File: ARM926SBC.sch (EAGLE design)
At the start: 53 parts, among them IC1 AT91SAM9260B-QU, IC2 LP2985IM5X-1.8, IC3 LM3671MF-1.8, IC4 LM3671MF-3.3, IC5 LP2985IM5X-3.3, Q1 2N7002, X1 16M, X2 32768

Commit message: Semi-finished: SDRAM and NAND
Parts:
- added IC6: MT48LC32M16A2-75C, ARM926SBC:MT48LC32M16A2-75C
- added IC7: K9F4G08U0B-P, ARM926SBC:K9F4G08U0B-P
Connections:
- new net A0: IC1-EBI.A2, IC6.A0
- new net A1: IC1-EBI.A3, IC6.A1
- new net A10: IC1-EBI.SDA10, IC6.A10
- new net A11: IC1-EBI.A13, IC6.A11
- new net A12: IC1-EBI.A14, IC6.A12
- new net A2: IC1-EBI.A4, IC6.A2
- new net A3: IC1-EBI.A5, IC6.A3
- new net A4: IC1-EBI.A6, IC6.A4
- new net A5: IC1-EBI.A7, IC6.A5
- new net A6: IC1-EBI.A8, IC6.A6
- new net A7: IC1-EBI.A9, IC6.A7
- new net A8: IC1-EBI.A10, IC6.A8
- new net A9: IC1-EBI.A11, IC6.A9
- new net BA0: IC1-EBI.A16/BA0, IC6.BA0
- new net BA1: IC1-EBI.A17/BA1, IC6.BA1
- new net CS0: IC1-EBI.CS#0
- new net CS1: IC1-EBI.CS#1, IC6.CS#
- new net CS3: IC1-PORTC.PC14/CS#3/IRQ2, IC7.CE#
- new net D0: IC1-EBI.D0, IC6.D0, IC7.D0
- new net D1: IC1-EBI.D1, IC6.D1, IC7.D1
- new net D10: IC1-EBI.D10, IC6.D10
- new net D11: IC1-EBI.D11, IC6.D11
- new net D12: IC1-EBI.D12, IC6.D12
- new net D13: IC1-EBI.D13, IC6.D13
- new net D14: IC1-EBI.D14, IC6.D14
- new net D15: IC1-EBI.D15, IC6.D15
- new net D2: IC1-EBI.D2, IC6.D2, IC7.D2
- new net D3: IC1-EBI.D3, IC6.D3, IC7.D3
- new net D4: IC1-EBI.D4, IC6.D4, IC7.D4
- new net D5: IC1-EBI.D5, IC6.D5, IC7.D5
- new net D6: IC1-EBI.D6, IC6.D6, IC7.D6
- new net D7: IC1-EBI.D7, IC6.D7, IC7.D7
- new net D8: IC1-EBI.D8, IC6.D8
- new net D9: IC1-EBI.D9, IC6.D9
- new net DQM0: IC1-EBI.BS#0/A0, IC6.DQML
- new net DQM1: IC1-EBI.BS#1/WR#1, IC6.DQMH
- new net DQM2: IC1-EBI.WR#2/BS#2/A1
- new net DQM3: IC1-EBI.BS#3/WR#3
- new net NALE: IC7.ALE
- new net NCLE: IC7.CLE
- new net NRD: IC1-EBI.NAND_RD, IC7.RD#
- new net NWR: IC1-EBI.NAND_WR, IC7.WR#
- new net SDCAS: IC1-EBI.CAS, IC6.CAS#
- new net SDCKE: IC1-EBI.SDCKE, IC6.CKE
- new net SDCLK: IC1-EBI.SDCK, IC6.CLK
- new net SDRAS: IC1-EBI.RAS, IC6.RAS#
- new net SDWE: IC1-EBI.SDWE, IC6.WE#
- new net SRD: IC1-EBI.RD#
- new net SWR: IC1-EBI.WR#
- net GND: now also IC6.GND, IC6.GNDQ, IC7.GND
- net VDD: now also IC6.VDD, IC6.VDDQ, IC7.VDD, IC7.WP#
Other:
- note added: "SDRAM and NAND"

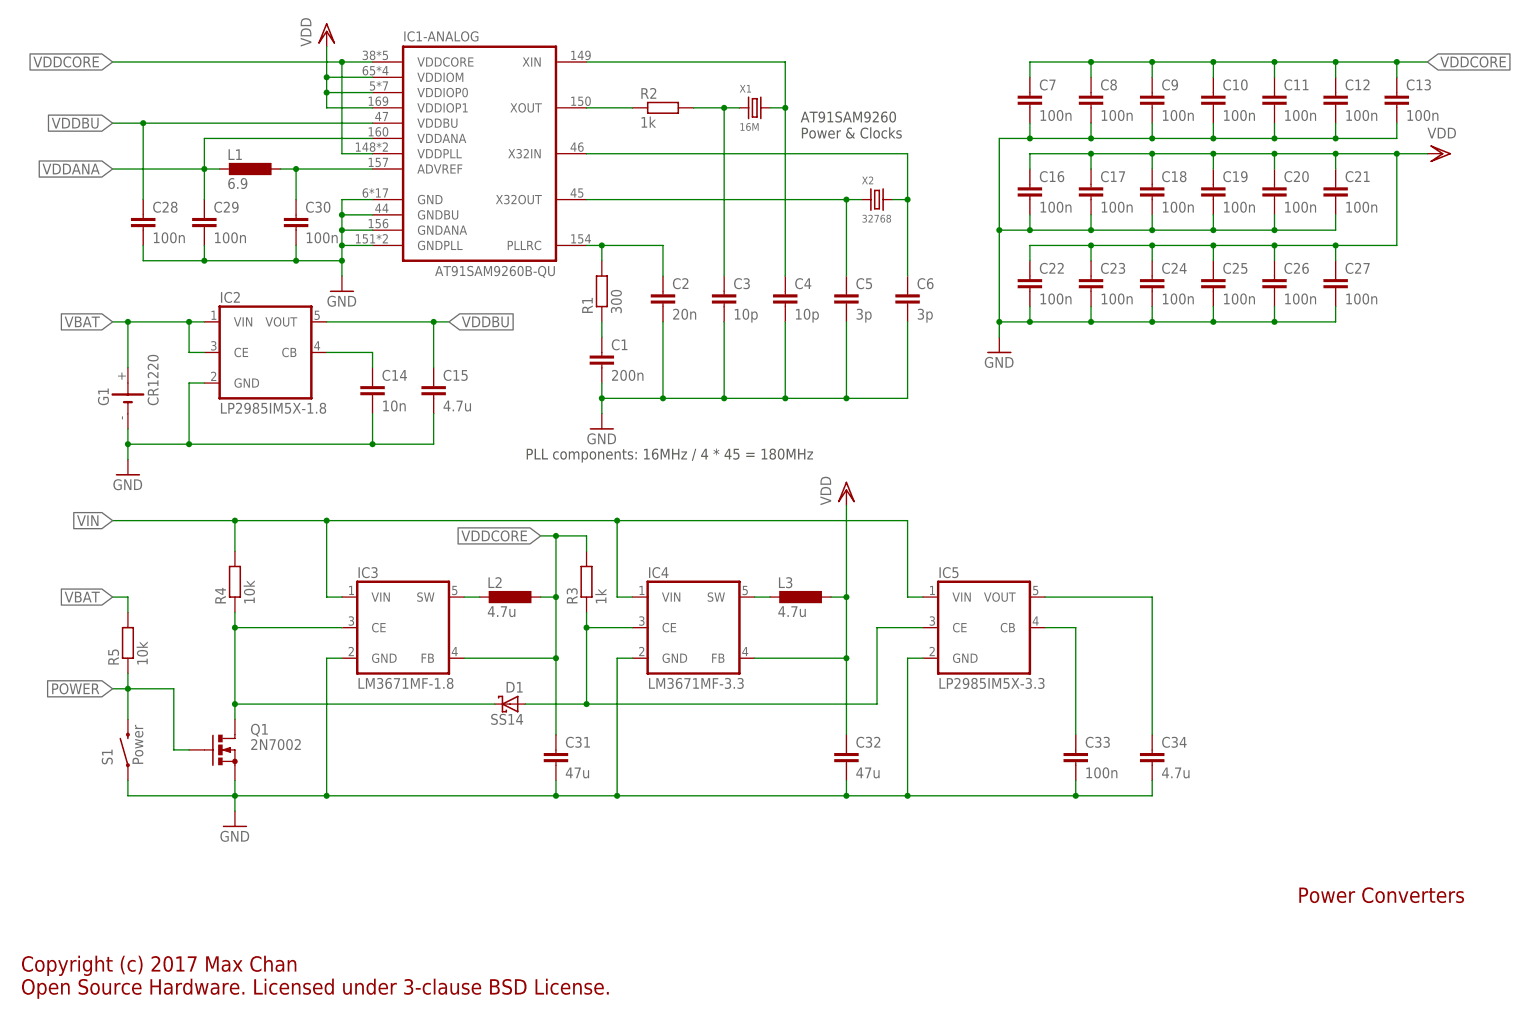
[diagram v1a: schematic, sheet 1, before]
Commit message: Renamed parts
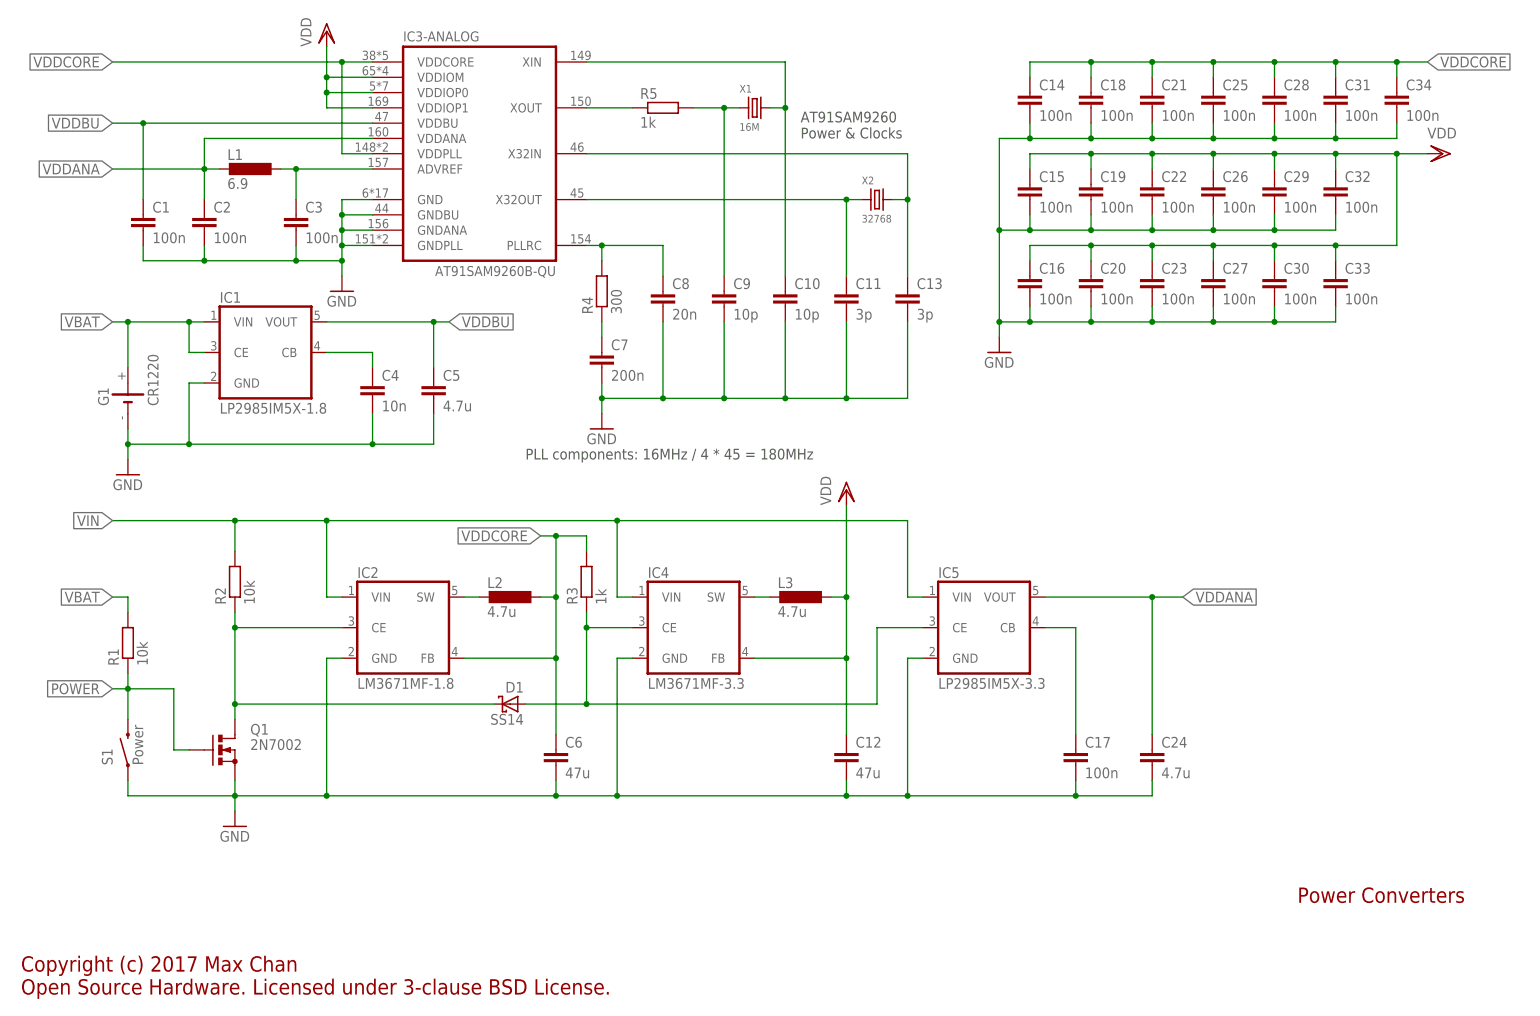
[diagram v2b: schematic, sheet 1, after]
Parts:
- C1: value 200n -> 100n
- C10, C9: value 100n -> 10p
- C11, C13: value 100n -> 3p
- C12: value 100n -> 47u; device rcl:C-EUC0603 -> rcl:C-EUC1206
- C14: value 10n -> 100n
- C15, C34: value 4.7u -> 100n
- C2: value 20n -> 100n
- C24: value 100n -> 4.7u
- C3: value 10p -> 100n
- C31, C32: value 47u -> 100n; device rcl:C-EUC1206 -> rcl:C-EUC0603
- C4: value 10p -> 10n
- C5: value 3p -> 4.7u
- C6: value 3p -> 47u; device rcl:C-EUC0603 -> rcl:C-EUC1206
- C7: value 100n -> 200n
- C8: value 100n -> 20n
- IC1: value AT91SAM9260B-QU -> LP2985IM5X-1.8; device ARM926SBC:AT91SAM9260B-QU -> ARM926SBC:LP2985IM5X-1.8
- IC2: value LP2985IM5X-1.8 -> LM3671MF-1.8; device ARM926SBC:LP2985IM5X-1.8 -> ARM926SBC:LM3671MF-1.8
- IC3: value LM3671MF-1.8 -> AT91SAM9260B-QU; device ARM926SBC:LM3671MF-1.8 -> ARM926SBC:AT91SAM9260B-QU
- R1: value 300 -> 10k
- R2: value 1k -> 10k
- R4: value 10k -> 300
- R5: value 10k -> 1k
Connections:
- removed net N$12: C34.1, IC5.VOUT
- net A0: now also IC3-EBI.A2; no longer IC1-EBI.A2
- net A1: now also IC3-EBI.A3; no longer IC1-EBI.A3
- net A10: now also IC3-EBI.SDA10; no longer IC1-EBI.SDA10
- net A11: now also IC3-EBI.A13; no longer IC1-EBI.A13
- net A12: now also IC3-EBI.A14; no longer IC1-EBI.A14
- net A2: now also IC3-EBI.A4; no longer IC1-EBI.A4
- net A3: now also IC3-EBI.A5; no longer IC1-EBI.A5
- net A4: now also IC3-EBI.A6; no longer IC1-EBI.A6
- net A5: now also IC3-EBI.A7; no longer IC1-EBI.A7
- net A6: now also IC3-EBI.A8; no longer IC1-EBI.A8
- net A7: now also IC3-EBI.A9; no longer IC1-EBI.A9
- net A8: now also IC3-EBI.A10; no longer IC1-EBI.A10
- net A9: now also IC3-EBI.A11; no longer IC1-EBI.A11
- net ADVREF: now also C3.1, IC3-ANALOG.ADVREF; no longer C30.1, IC1-ANALOG.ADVREF
- net BA0: now also IC3-EBI.A16/BA0; no longer IC1-EBI.A16/BA0
- net BA1: now also IC3-EBI.A17/BA1; no longer IC1-EBI.A17/BA1
- net CS0: now also IC3-EBI.CS#0; no longer IC1-EBI.CS#0
- net CS1: now also IC3-EBI.CS#1; no longer IC1-EBI.CS#1
- net CS3: now also IC3-PORTC.PC14/CS#3/IRQ2; no longer IC1-PORTC.PC14/CS#3/IRQ2
- net D0: now also IC3-EBI.D0; no longer IC1-EBI.D0
- net D1: now also IC3-EBI.D1; no longer IC1-EBI.D1
- net D10: now also IC3-EBI.D10; no longer IC1-EBI.D10
- net D11: now also IC3-EBI.D11; no longer IC1-EBI.D11
- net D12: now also IC3-EBI.D12; no longer IC1-EBI.D12
- net D13: now also IC3-EBI.D13; no longer IC1-EBI.D13
- net D14: now also IC3-EBI.D14; no longer IC1-EBI.D14
- net D15: now also IC3-EBI.D15; no longer IC1-EBI.D15
- net D2: now also IC3-EBI.D2; no longer IC1-EBI.D2
- net D3: now also IC3-EBI.D3; no longer IC1-EBI.D3
- net D4: now also IC3-EBI.D4; no longer IC1-EBI.D4
- net D5: now also IC3-EBI.D5; no longer IC1-EBI.D5
- net D6: now also IC3-EBI.D6; no longer IC1-EBI.D6
- net D7: now also IC3-EBI.D7; no longer IC1-EBI.D7
- net D8: now also IC3-EBI.D8; no longer IC1-EBI.D8
- net D9: now also IC3-EBI.D9; no longer IC1-EBI.D9
- net DQM0: now also IC3-EBI.BS#0/A0; no longer IC1-EBI.BS#0/A0
- net DQM1: now also IC3-EBI.BS#1/WR#1; no longer IC1-EBI.BS#1/WR#1
- net DQM2: now also IC3-EBI.WR#2/BS#2/A1; no longer IC1-EBI.WR#2/BS#2/A1
- net DQM3: now also IC3-EBI.BS#3/WR#3; no longer IC1-EBI.BS#3/WR#3
- net GND: now also IC1.GND, IC3-ANALOG.GND, IC3-ANALOG.GNDANA, IC3-ANALOG.GNDBU, IC3-ANALOG.GNDPLL; no longer IC1-ANALOG.GND, IC1-ANALOG.GNDANA, IC1-ANALOG.GNDBU, IC1-ANALOG.GNDPLL, IC3.GND
- net N$1: now also C8.1, IC3-ANALOG.PLLRC, R4.2; no longer C2.1, IC1-ANALOG.PLLRC, R1.2
- net N$11: now also IC2.SW; no longer IC3.SW
- net N$14: now also C17.1; no longer C33.1
- net N$15: now also IC2.CE, R2.1; no longer IC3.CE, R4.1
- net N$2: now also C7.1, R4.1; no longer C1.1, R1.1
- net N$3: now also IC3-ANALOG.XOUT, R5.1; no longer IC1-ANALOG.XOUT, R2.1
- net N$4: now also C9.1, R5.2; no longer C3.1, R2.2
- net N$5: now also C10.1, IC3-ANALOG.XIN; no longer C4.1, IC1-ANALOG.XIN
- net N$6: now also C11.1, IC3-ANALOG.X32OUT; no longer C5.1, IC1-ANALOG.X32OUT
- net N$7: now also C13.1, IC3-ANALOG.X32IN; no longer C6.1, IC1-ANALOG.X32IN
- net N$9: now also C4.1, IC1.CB; no longer C14.1, IC2.CB
- net NRD: now also IC3-EBI.NAND_RD; no longer IC1-EBI.NAND_RD
- net NWR: now also IC3-EBI.NAND_WR; no longer IC1-EBI.NAND_WR
- net POWER: now also R1.1; no longer R5.1
- net SDCAS: now also IC3-EBI.CAS; no longer IC1-EBI.CAS
- net SDCKE: now also IC3-EBI.SDCKE; no longer IC1-EBI.SDCKE
- net SDCLK: now also IC3-EBI.SDCK; no longer IC1-EBI.SDCK
- net SDRAS: now also IC3-EBI.RAS; no longer IC1-EBI.RAS
- net SDWE: now also IC3-EBI.SDWE; no longer IC1-EBI.SDWE
- net SRD: now also IC3-EBI.RD#; no longer IC1-EBI.RD#
- net SWR: now also IC3-EBI.WR#; no longer IC1-EBI.WR#
- net VBAT: now also IC1.CE, IC1.VIN, R1.2; no longer IC2.CE, IC2.VIN, R5.2
- net VDD: now also C12.1, C15.1, C29.1, C30.1, C33.1, IC3-ANALOG.VDDIOM, IC3-ANALOG.VDDIOP0, IC3-ANALOG.VDDIOP1; no longer C17.1, C18.1, C21.1, C24.1, C25.1, IC1-ANALOG.VDDIOM, IC1-ANALOG.VDDIOP0, IC1-ANALOG.VDDIOP1
- net VDDANA: now also C2.1, C24.1, IC3-ANALOG.VDDANA, IC5.VOUT; no longer C29.1, IC1-ANALOG.VDDANA
- net VDDBU: now also C1.1, C5.1, IC1.VOUT, IC3-ANALOG.VDDBU; no longer C15.1, C28.1, IC1-ANALOG.VDDBU, IC2.VOUT
- net VDDCORE: now also C14.1, C18.1, C21.1, C25.1, C28.1, C34.1, C6.1, IC2.FB, IC3-ANALOG.VDDCORE, IC3-ANALOG.VDDPLL; no longer C10.1, C11.1, C12.1, C13.1, C7.1, C8.1, C9.1, IC1-ANALOG.VDDCORE, IC1-ANALOG.VDDPLL, IC3.FB
- net VIN: now also IC2.VIN, R2.2; no longer IC3.VIN, R4.2
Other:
- moved on the sheet: C1, C10, C11, C12, C13, C14, C15, C16, C17, C18, C19, C2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

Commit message: Added some connectivity stuff.
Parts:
- added IC10: 25AA02E48-SN, ARM926SBC:25AA02E48-SN
- added IC8: RTL8201CL, ARM926SBC:RTL8201CL
- added IC9: AT45DB321E-S, ARM926SBC:AT45DB321E-S
- added J1: USD-HOLDER, ARM926SBC:USD-HOLDER
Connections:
- new net ECOL: IC3-PORTA.PA29/SCK1/ECOL, IC8.COL
- new net ECRS: IC3-PORTA.PA28/TIOA2/ECRS, IC8.CRS
- new net EMDC: IC3-PORTA.PA20/EMDC, IC8.MDC
- new net EMDIO: IC3-PORTA.PA21/EMDIO, IC8.MDIO
- new net ERXC: IC3-PORTA.PA27/TIOA1/ERXCK, IC8.RXC
- new net ERXD0: IC3-PORTA.PA14/ERX0, IC8.RXD0
- new net ERXD1: IC3-PORTA.PA15/ERX1, IC8.RXD1
- new net ERXD2: IC3-PORTA.PA25/TCLK0/ERX2, IC8.RXD2
- new net ERXD3: IC3-PORTA.PA26/TIOA0/ERX3, IC8.RXD3
- new net ERXDV: IC3-PORTA.PA17/ERXDV, IC8.RXDV
- new net ERXER: IC3-PORTA.PA18/ERXER, IC8.RXER/FXEN
- new net ETXC: IC3-PORTA.PA19/ETXCK, IC8.TXC
- new net ETXD0: IC3-PORTA.PA12/ETX0, IC8.TXD0
- new net ETXD1: IC3-PORTA.PA13/ETX1, IC8.TXD1
- new net ETXD2: IC3-PORTA.PA23/TWD/ETX2, IC8.TXD2
- new net ETXD3: IC3-PORTA.PA24/TWCK/ETX3, IC8.TXD3
- new net ETXEN: IC3-PORTA.PA16/ETXEN, IC8.TXEN
- new net S0-CS0: IC3-PORTA.PA3/SPI0_CS0/MCDB3, IC9.CS#
- new net S0-CS1: IC10.CS#
- new net S0-MISO: IC10.MISO, IC3-PORTA.PA0/SPI0_MISO/MCDB0, IC9.MISO
- new net S0-MOSI: IC10.MOSI, IC3-PORTA.PA1/SPI0_MOSI/MCCDB, IC9.MOSI
- new net S0-SCK: IC10.SCK, IC3-PORTA.PA2/SPI0_SCK, IC9.SCK
- new net SDCK: IC3-PORTA.PA8/MCCK, J1.CLK
- new net SDCMD: IC3-PORTA.PA7/MCCDA, J1.CMD
- new net SDD0: IC3-PORTA.PA6/MCDA0, J1.DAT0
- new net SDD1: IC3-PORTA.PA9/MCDA1, J1.DAT1
- new net SDD2: IC3-PORTA.PA10/MCDA2/ETX2, J1.DAT2
- new net SDD3: IC3-PORTA.PA11/MCDA3/ETX3, J1.CD/DAT3
- net CS3: no longer IC3-PORTC.PC14/CS#3/IRQ2
- net GND: now also IC10.GND, IC9.GND, J1.GND, J1.SHIELD
- net NALE: now also IC3-EBI.A21
- net NCLE: now also IC3-EBI.A22
- net VDD: now also IC10.HOLD#, IC10.VDD, IC10.WP#, IC9.RESET#, IC9.VDD, IC9.WP#, J1.VCC
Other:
- note added: "Connectivity"
